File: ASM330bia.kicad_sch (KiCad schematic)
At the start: 7 parts, among them J1 Conn_01x06_Pin, U1 ASM330LHH

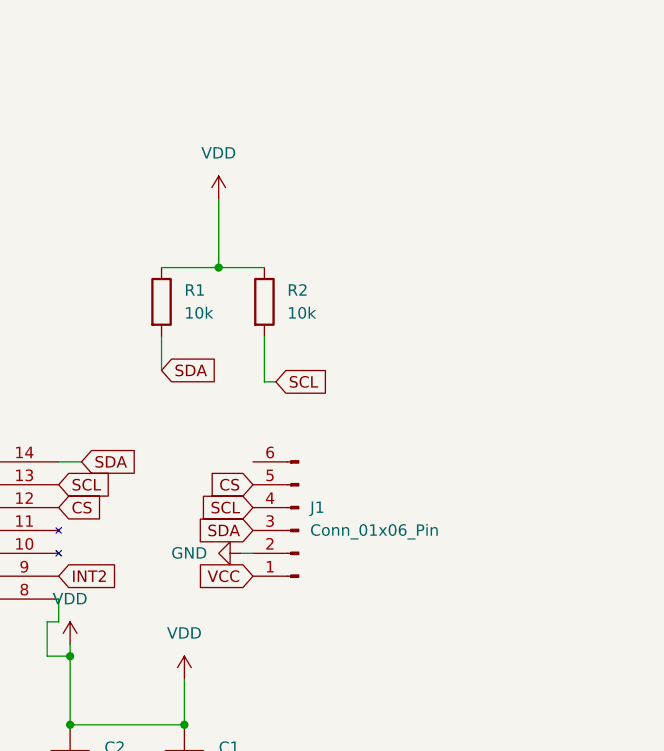
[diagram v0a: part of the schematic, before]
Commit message: Att
Adicionado interrupts e revisado design pcb e alimentação
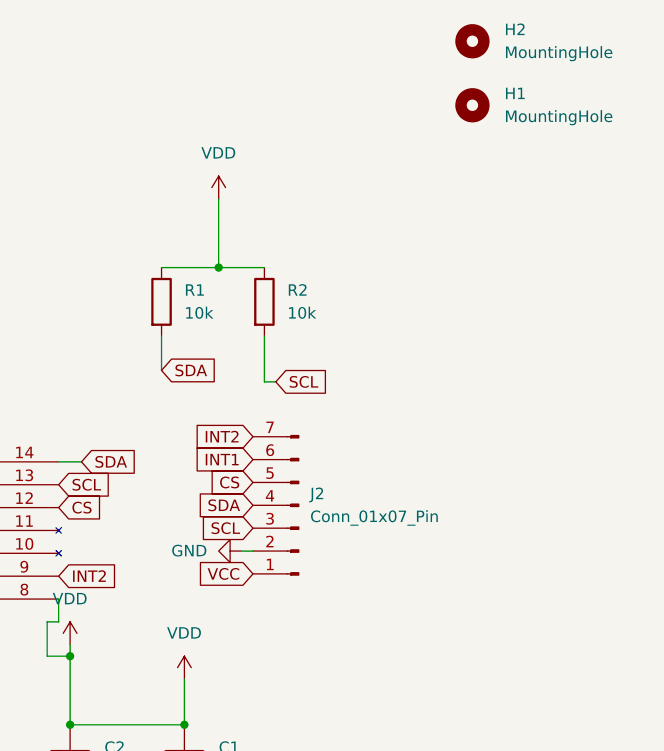
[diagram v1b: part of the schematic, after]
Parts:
- removed J1: Conn_01x06_Pin, Connector_PinSocket_2.54mm:PinSocket_1x06_P2.54mm_Vertical, symbol Connector:Conn_01x06_Pin
- added H1, H2: MountingHole, MountingHole:MountingHole_2.7mm, symbol Mechanical:MountingHole
- added J2: Conn_01x07_Pin, Connector_PinSocket_2.54mm:PinSocket_1x07_P2.54mm_Vertical, symbol Connector:Conn_01x07_Pin
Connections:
- net CS: now also J2.5 (Pin_5)
- net GND: now also J2.2 (Pin_2)
- net INT1: now also J2.6 (Pin_6)
- net INT2: now also J2.7 (Pin_7)
- net SCL: now also J2.3 (Pin_3)
- net SDA: now also J2.4 (Pin_4)
- net VDD: now also J2.1 (Pin_1)

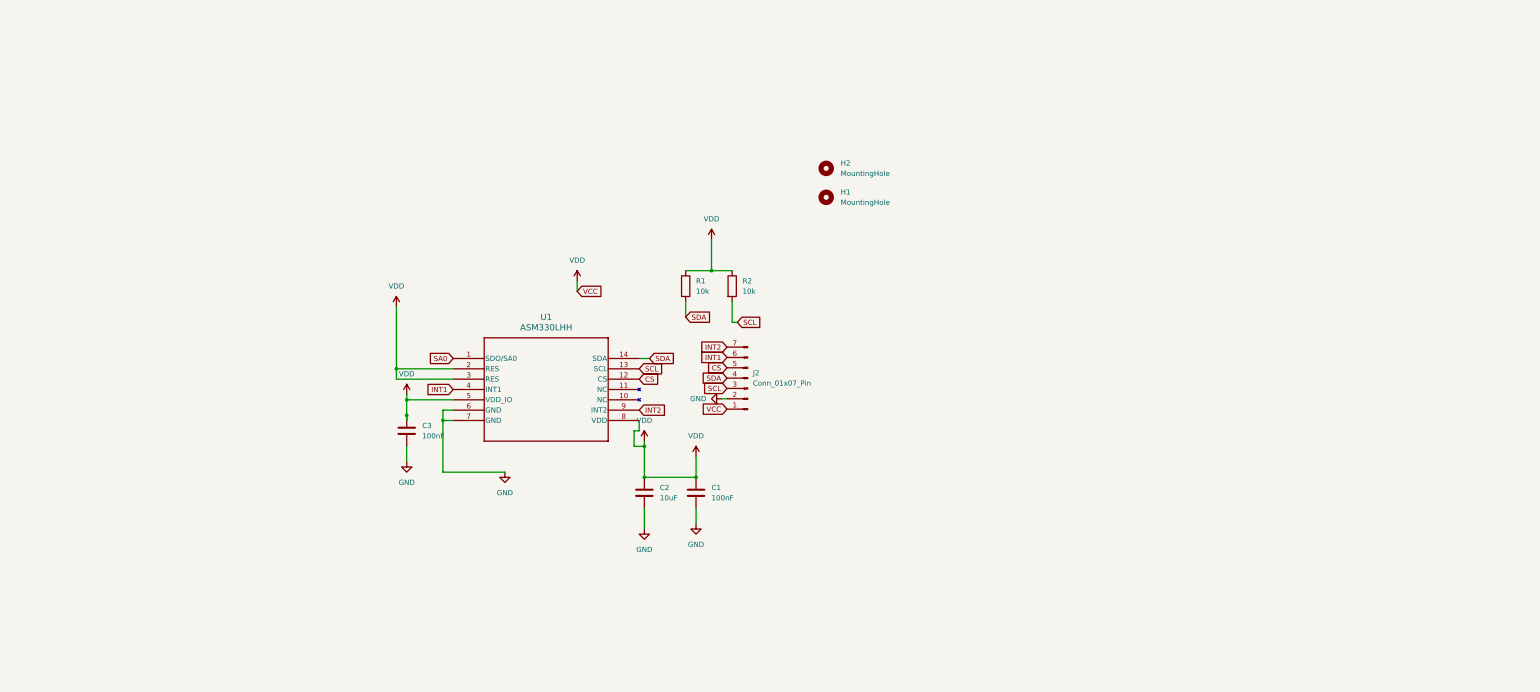
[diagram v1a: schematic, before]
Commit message: Adição ESP32-S3 e modulo SDCARD
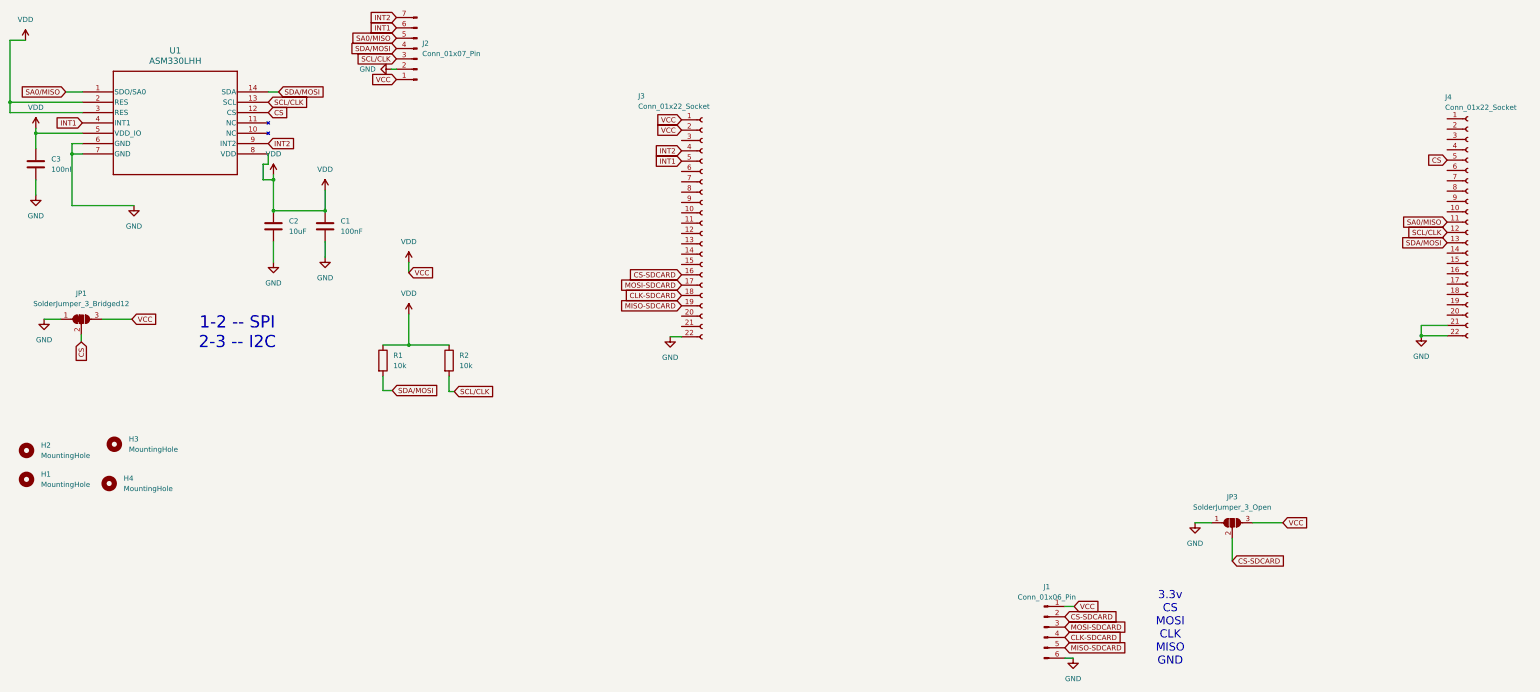
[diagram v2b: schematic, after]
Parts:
- added H3, H4: MountingHole, MountingHole:MountingHole_2.7mm, symbol Mechanical:MountingHole
- added J1: Conn_01x06_Pin, Connector_PinHeader_2.54mm:PinHeader_1x06_P2.54mm_Vertical, symbol Connector:Conn_01x06_Pin
- added J3, J4: Conn_01x22_Socket, Connector_PinHeader_2.54mm:PinHeader_1x22_P2.54mm_Vertical, symbol Connector:Conn_01x22_Socket
- added JP1: SolderJumper_3_Bridged12, Jumper:SolderJumper-3_P1.3mm_Bridged12_RoundedPad1.0x1.5mm, symbol Jumper:SolderJumper_3_Bridged12
- added JP3: SolderJumper_3_Open, Jumper:SolderJumper-3_P1.3mm_Open_RoundedPad1.0x1.5mm, symbol Jumper:SolderJumper_3_Open
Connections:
- net CS: now also J4.5 (Pin_5), JP1.2 (C); no longer J2.5 (Pin_5)
- net GND: now also J1.6 (Pin_6), J3.22 (Pin_22), J4.21 (Pin_21), J4.22 (Pin_22), JP1.1 (A), JP3.1 (A)
- net INT1: now also J3.5 (Pin_5)
- net INT2: now also J3.4 (Pin_4)
- net VDD: now also J1.1 (Pin_1), J3.1 (Pin_1), J3.2 (Pin_2), JP1.3 (B), JP3.3 (B)
- net SA0 renamed SA0/MISO
- net SA0/MISO: now also J2.5 (Pin_5), J4.11 (Pin_11)
- net SCL renamed SCL/CLK
- net SCL/CLK: now also J4.12 (Pin_12)
- net SDA renamed SDA/MOSI
- net SDA/MOSI: now also J4.13 (Pin_13)
- new net CLK-SDCARD: J1.4 (Pin_4), J3.18 (Pin_18)
- new net CS-SDCARD: J1.2 (Pin_2), J3.16 (Pin_16), JP3.2 (C)
- new net MISO-SDCARD: J1.5 (Pin_5), J3.19 (Pin_19)
- new net MOSI-SDCARD: J1.3 (Pin_3), J3.17 (Pin_17)
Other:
- note added: "1-2 -- SPI 2-3 -- I2C"
- note added: "3.3v CS MOSI CLK MISO GND"
- moved on the sheet: C1, C2, C3, H1, H2, J2, R1, R2, U1
